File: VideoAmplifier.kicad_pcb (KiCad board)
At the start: 2 copper layers, 24 parts, among them IC1 THS7374IPWR, J1 Signal In, J2 Power In, J3 Signal Out

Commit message: adding text to the back of the board
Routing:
- net +5V: track 48.0 -> 45.8 mm
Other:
- board outline added: 69.8 x 36.8 mm
- board text added: "Video Amplifier v0.1 anders@conbere.org"
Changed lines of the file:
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@@
   (general
     (thickness 1.6)
-    (drawings 0)
-    (tracks 77)
+    (drawings 5)
+    (tracks 75)
     (zones 0)
     (modules 24)
@@
   (setup
     (last_trace_width 0.25)
+    (user_trace_width 0.254)
+    (user_trace_width 0.508)
     (trace_clearance 0.2)
     (zone_clearance 0.508)
@@
     (solder_mask_min_width 0.25)
     (aux_axis_origin 0 0)
-    (visible_elements FFFFFF7F)
+    (visible_elements 7FFFFFFF)
     (pcbplotparams
       (layerselection 0x010fc_ffffffff)
@@
     )
   )
+  (gr_text "Video Amplifier v0.1\nanders@conbere.org" (at 133.35 72.39) (layer B.SilkS)
+    (effects (font (size 1 1) (thickness 0.15)) (justify mirror))
+  )
+  (gr_line (start 97.79 44.45) (end 167.64 44.45) (layer Edge.Cuts) (width 0.05))
+  (gr_line (start 97.79 81.28) (end 97.79 44.45) (layer Edge.Cuts) (width 0.05))
+  (gr_line (start 167.64 81.28) (end 97.79 81.28) (layer Edge.Cuts) (width 0.05))
+  (gr_line (start 167.64 44.45) (end 167.64 81.28) (layer Edge.Cuts) (width 0.05))
   (segment (start 127.872 55.522) (end 123.15 50.8) (width 0.25) (layer F.Cu) (net 1))
   (segment (start 127.872 59.01) (end 127.872 55.522) (width 0.25) (layer F.Cu) (net 1))
@@
   (segment (start 127.872 62.26) (end 126.8845 62.26) (width 0.25) (layer F.Cu) (net 17))
   (segment (start 133.748 62.26) (end 134.7355 62.26) (width 0.25) (layer F.Cu) (net 17))
+  (segment (start 103.369002 76.2) (end 102.6 76.2) (width 0.25) (layer F.Cu) (net 20))
   (segment (start 102.6 76.2) (end 101.6 76.2) (width 0.25) (layer F.Cu) (net 20))
-  (segment (start 103.369002 76.2) (end 102.6 76.2) (width 0.25) (layer F.Cu) (net 20))
+  (segment (start 135.26051 66.728492) (end 123.494001 78.495001) (width 0.25) (layer F.Cu) (net 20))
+  (segment (start 135.26051 62.13501) (end 135.26051 66.728492) (width 0.25) (layer F.Cu) (net 20))
+  (segment (start 134.7355 61.61) (end 135.26051 62.13501) (width 0.25) (layer F.Cu) (net 20))
+  (segment (start 105.664003 78.495001) (end 103.369002 76.2) (width 0.25) (layer F.Cu) (net 20))
   (segment (start 123.494001 78.495001) (end 105.664003 78.495001) (width 0.25) (layer F.Cu) (net 20))
-  (segment (start 105.664003 78.495001) (end 103.369002 76.2) (width 0.25) (layer F.Cu) (net 20))
-  (segment (start 136.615001 65.374001) (end 123.494001 78.495001) (width 0.25) (layer F.Cu) (net 20))
-  (segment (start 136.615001 61.881999) (end 136.615001 65.374001) (width 0.25) (layer F.Cu) (net 20))
-  (segment (start 136.238001 61.504999) (end 136.615001 61.881999) (width 0.25) (layer F.Cu) (net 20))
-  (segment (start 134.840501 61.504999) (end 136.238001 61.504999) (width 0.25) (layer F.Cu) (net 20))
-  (segment (start 134.7355 61.61) (end 134.840501 61.504999) (width 0.25) (layer F.Cu) (net 20))
   (segment (start 133.748 61.61) (end 134.7355 61.61) (width 0.25) (layer F.Cu) (net 20))
   (segment (start 141.540001 75.500001) (end 142.24 76.2) (width 0.25) (layer F.Cu) (net 21))

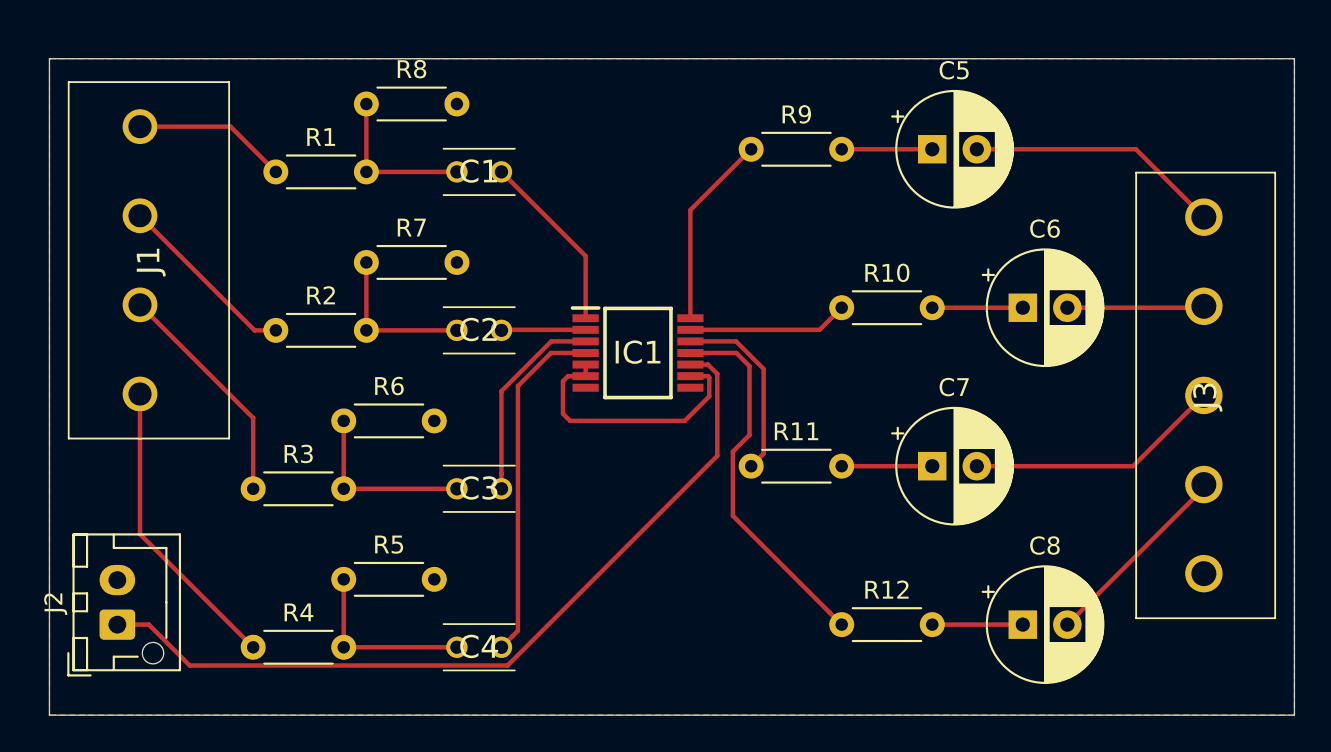
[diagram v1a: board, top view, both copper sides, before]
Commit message: updates for printing
added mounting holes, made the tolerances a bit tighter.
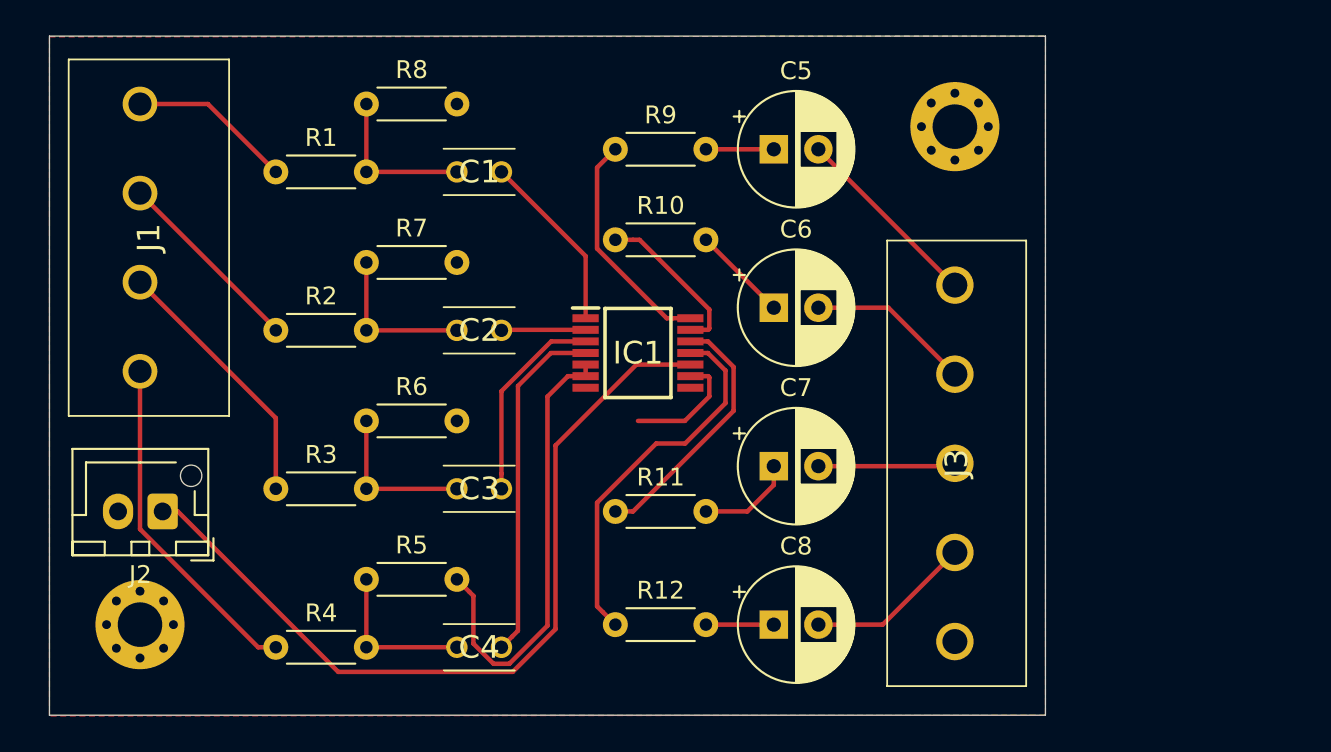
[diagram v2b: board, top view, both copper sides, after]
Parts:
- added REF**: MountingHole_2.5mm_Pad_Via, MountingHole:MountingHole_2.5mm_Pad_Via, F.Cu at (102.9, 76.2)
- added REF**: MountingHole_2.5mm_Pad_Via, MountingHole:MountingHole_2.5mm_Pad_Via, F.Cu at (148.6, 48.3)
- moved J3 14.5 mm to (148.6, 57.1)
- moved C6 14.0 mm to (138.4, 58.4)
- moved C8 14.0 mm to (138.4, 76.2)
- moved R10 13.3 mm to (129.5, 54.6)
- moved R12 12.7 mm to (129.5, 76.2)
- moved C5 8.89 mm to (138.4, 49.5)
- moved C7 8.89 mm to (138.4, 67.3)
- moved R11 8.03 mm to (129.5, 69.8)
- moved R9 7.62 mm to (129.5, 49.5)
- moved J2 6.84 mm to (104.1, 69.8), turned to 180 degrees
- moved J1 1.27 mm to (102.9, 47.0)
- moved R3 1.27 mm to (110.5, 68.6)
- moved R4 1.27 mm to (110.5, 77.5)
- moved R5 1.27 mm to (115.6, 73.7)
- moved R6 1.27 mm to (115.6, 64.8)
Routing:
- net GND: track 15.0 -> 32.3 mm
- net /Blue-Out: track 14.4 -> 7.73 mm
- net Net-(IC1-Pad12): track 10.5 -> 14.5 mm
- net /Red-Out: track 14.3 -> 10.8 mm
- net /Sync-In: track 16.8 -> 19.2 mm
- net Net-(IC1-Pad14): track 10.9 -> 12.9 mm
- net /Blue-In: track 13.0 -> 14.7 mm
- net /Sync-Out: track 11.0 -> 9.34 mm
- net /Green-Out: track 7.69 -> 9.21 mm
- net Net-(C8-Pad1): track 5.08 -> 3.81 mm
- net Net-(C4-Pad1): track 10.2 -> 8.89 mm
- net Net-(C3-Pad1): track 10.2 -> 8.89 mm
- net Net-(C5-Pad1): track 5.08 -> 3.81 mm
- net +5V: track 45.8 -> 46.5 mm
- net /Green-In: track 10.3 -> 10.9 mm
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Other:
- board size 69.8 x 36.8 mm -> 55.9 x 38.1 mm

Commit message: update track clearances for oshpark
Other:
- net class Default: clearance 0.2 -> 0.1524; trace_width 0.25 -> 0.1524; via_dia 0.8 -> 0.6858; via_drill 0.4 -> 0.3302
- rule trace_clearance: 0.2 -> 0.1524
- rule trace_min: 0.2 -> 0.1524
- rule via_min_drill: 0.3 -> 0.254
- rule via_min_size: 0.4 -> 0.508
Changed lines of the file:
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@@
   )
   (setup
-    (last_trace_width 0.25)
+    (last_trace_width 0.1524)
     (user_trace_width 0.254)
     (user_trace_width 0.508)
-    (trace_clearance 0.2)
+    (trace_clearance 0.1524)
     (zone_clearance 0.508)
     (zone_45_only no)
-    (trace_min 0.2)
-    (via_size 0.8)
-    (via_drill 0.4)
-    (via_min_size 0.4)
-    (via_min_drill 0.3)
-    (uvia_size 0.3)
-    (uvia_drill 0.1)
+    (trace_min 0.1524)
+    (via_size 0.6858)
+    (via_drill 0.3302)
+    (via_min_size 0.508)
+    (via_min_drill 0.254)
+    (uvia_size 0.6858)
+    (uvia_drill 0.3302)
     (uvias_allowed no)
-    (uvia_min_size 0.2)
-    (uvia_min_drill 0.1)
+    (uvia_min_size 0.6858)
+    (uvia_min_drill 0.3302)
     (edge_width 0.05)
     (segment_width 0.2)
@@
   (net 28 /Sync-In)
   (net_class Default "This is the default net class."
-    (clearance 0.2)
-    (trace_width 0.25)
-    (via_dia 0.8)
-    (via_drill 0.4)
-    (uvia_dia 0.3)
-    (uvia_drill 0.1)
+    (clearance 0.1524)
+    (trace_width 0.1524)
+    (via_dia 0.6858)
+    (via_drill 0.3302)
+    (uvia_dia 0.6858)
+    (uvia_drill 0.3302)
     (add_net +5V)
     (add_net /Blue-In)
